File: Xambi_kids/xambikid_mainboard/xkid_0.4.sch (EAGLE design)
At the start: 18 parts

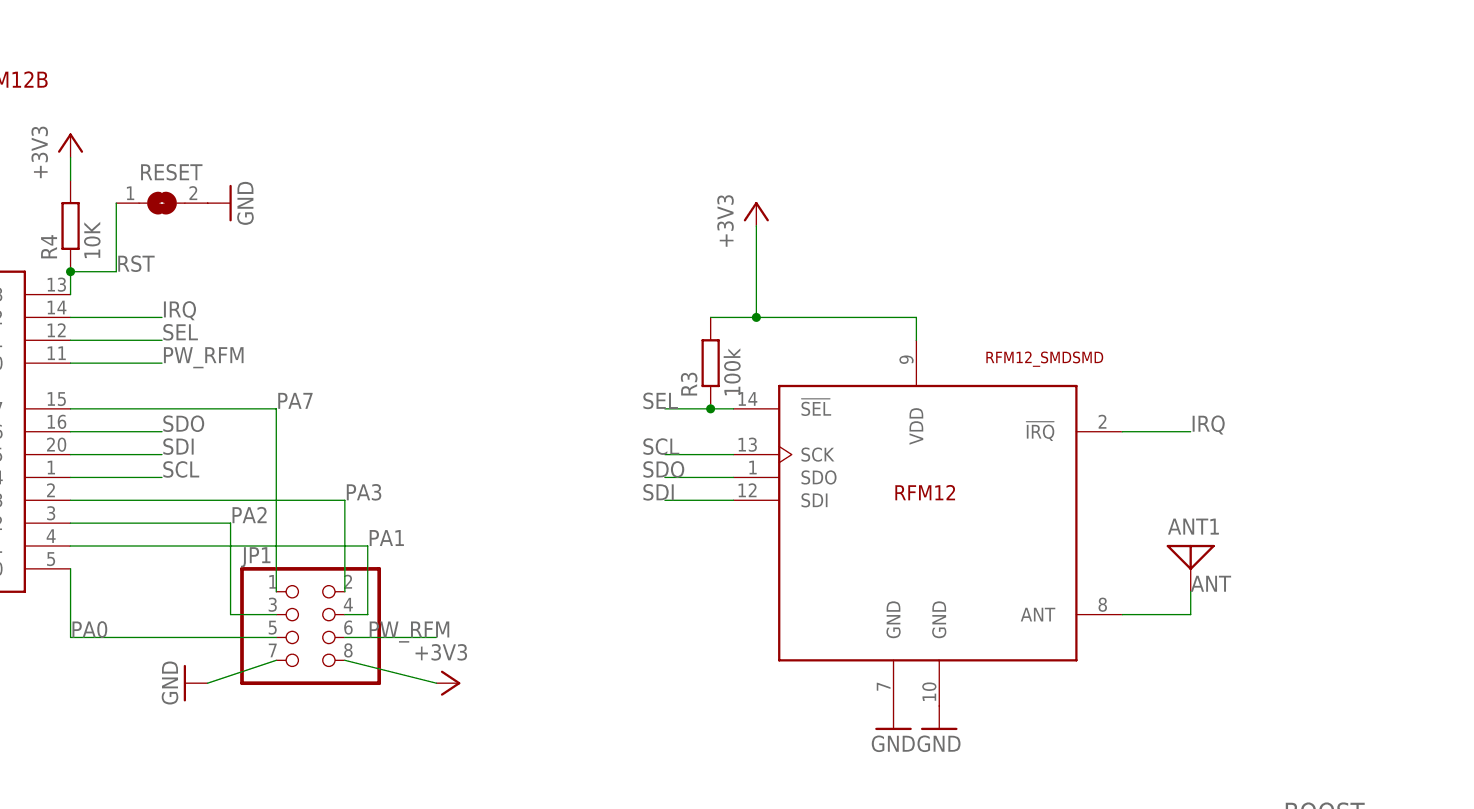
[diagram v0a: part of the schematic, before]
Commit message: - Add readme and pics to new board with booster and infrared
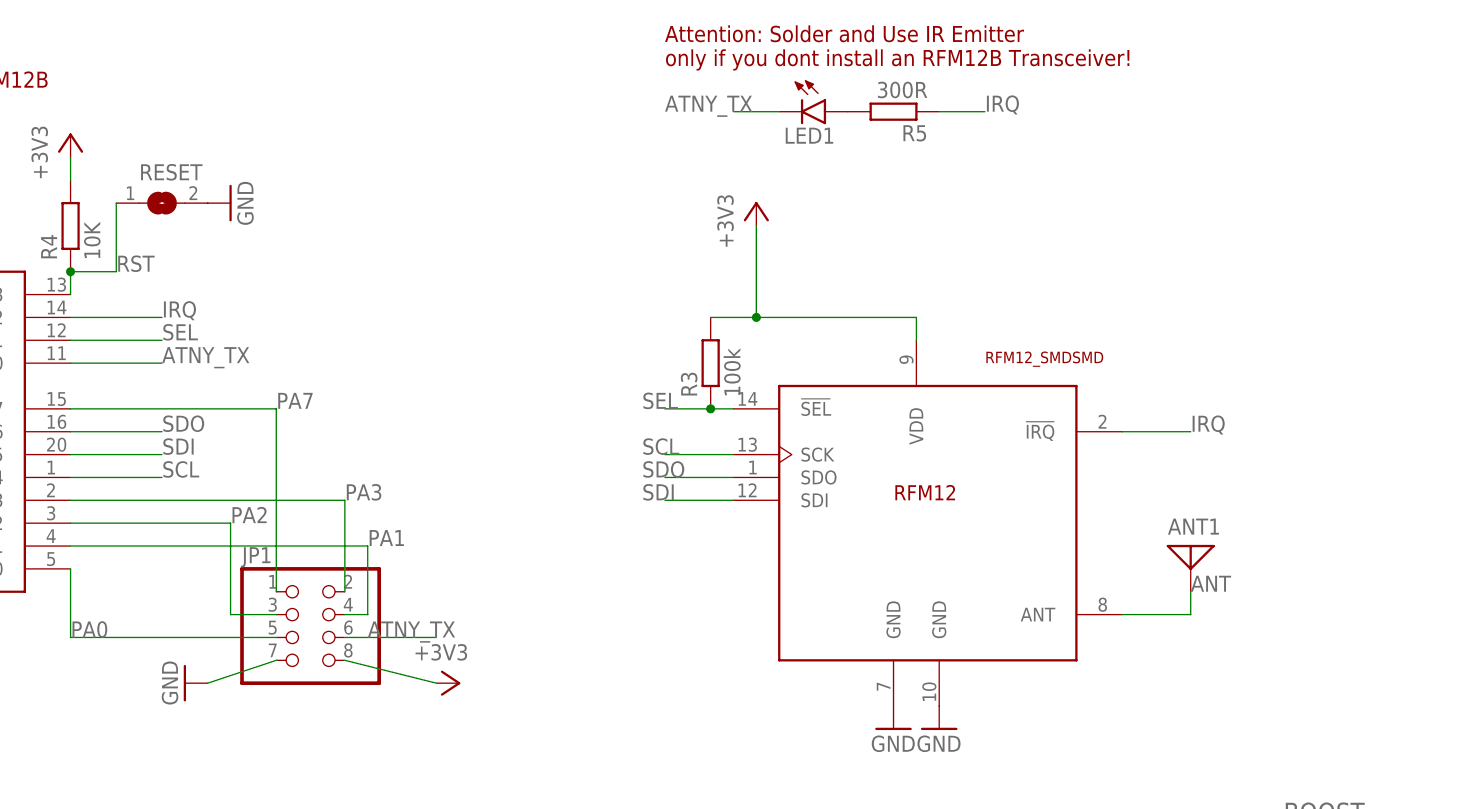
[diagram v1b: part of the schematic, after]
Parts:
- added LED1: (no value), SparkFun-LED:LED3MM
- added R5: 300R, rcl:R-EU_R0805
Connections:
- new net ATNY_TX: JP1.6, LED1.C, TINY84.(PCINT8/XTAL1/CLKI)PB0
- new net N$1: LED1.A, R5.2
- net IRQ: now also R5.1
- net PW_RFM: no longer JP1.6, TINY84.(PCINT8/XTAL1/CLKI)PB0
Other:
- note added: "Attention: Solder and Use IR Emitter only if you dont install an RFM12B Transceiver!"
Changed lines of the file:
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@@
 <?xml version="1.0" encoding="utf-8"?>
 <!DOCTYPE eagle SYSTEM "eagle.dtd">
-<eagle version="7.1.0">
+<eagle version="7.2.0">
 <drawing>
 <settings>
@@
 <part name="C4" library="rcl" deviceset="C-EU" device="C0805K" value="4.7mF"/>
 <part name="C5" library="rcl" deviceset="C-EU" device="C0805K" value="4.7mF"/>
+<part name="LED1" library="SparkFun-LED" deviceset="LED" device="3MM"/>
+<part name="R5" library="rcl" deviceset="R-EU_" device="R0805" value="300R"/>
 </parts>
 <sheets>
@@
 <text x="10.16" y="101.6" size="1.778" layer="94">Xambi_kid an attiny84 low power with a coincell CR2032 and a RFM12B
 http://jeelabs.net/projects/hardware/wiki/JeeNode_Micro</text>
+<text x="157.48" y="106.68" size="1.778" layer="94">Attention: Solder and Use IR Emitter
+only if you dont install an RFM12B Transceiver!</text>
 </plain>
 <instances>
@@
 <instance part="C4" gate="G$1" x="261.62" y="7.62" rot="R180"/>
 <instance part="C5" gate="G$1" x="195.58" y="5.08" rot="R180"/>
+<instance part="LED1" gate="G$1" x="175.26" y="101.6" rot="R270"/>
+<instance part="R5" gate="G$1" x="182.88" y="101.6" rot="R180"/>
 </instances>
 <busses>
@@
 <pinref part="U$1" gate="U$1" pin="!IRQ"/>
 </segment>
+<segment>
+<pinref part="R5" gate="G$1" pin="1"/>
+<wire x1="187.96" y1="101.6" x2="193.04" y2="101.6" width="0.1524" layer="91"/>
+<label x="193.04" y="101.6" size="1.778" layer="95"/>
+</segment>
 </net>
 <net name="RST" class="0">
@@
 </net>
 <net name="PW_RFM" class="0">
-<segment>
-<wire x1="91.44" y1="73.66" x2="101.6" y2="73.66" width="0.1524" layer="91"/>
-<label x="101.6" y="73.66" size="1.778" layer="95"/>
-<pinref part="TINY84" gate="G$1" pin="(PCINT8/XTAL1/CLKI)PB0"/>
-</segment>
-<segment>
-<pinref part="JP1" gate="A" pin="6"/>
-<wire x1="121.92" y1="43.18" x2="132.08" y2="43.18" width="0.1524" layer="91"/>
-<label x="124.46" y="43.18" size="1.778" layer="95"/>
-</segment>
 <segment>
 <pinref part="BOOST" gate="A" pin="VOUT"/>
@@
 </segment>
 </net>
+<net name="N$1" class="0">
+<segment>
+<pinref part="LED1" gate="G$1" pin="A"/>
+<pinref part="R5" gate="G$1" pin="2"/>
+</segment>
+</net>
+<net name="ATNY_TX" class="0">
+<segment>
+<wire x1="91.44" y1="73.66" x2="101.6" y2="73.66" width="0.1524" layer="91"/>
+<label x="101.6" y="73.66" size="1.778" layer="95"/>
+<pinref part="TINY84" gate="G$1" pin="(PCINT8/XTAL1/CLKI)PB0"/>
+</segment>
+<segment>
+<pinref part="JP1" gate="A" pin="6"/>
+<wire x1="121.92" y1="43.18" x2="132.08" y2="43.18" width="0.1524" layer="91"/>
+<label x="124.46" y="43.18" size="1.778" layer="95"/>
+</segment>
+<segment>
+<pinref part="LED1" gate="G$1" pin="C"/>
+<wire x1="170.18" y1="101.6" x2="165.1" y2="101.6" width="0.1524" layer="91"/>
+<label x="157.48" y="101.6" size="1.778" layer="95"/>
+</segment>
+</net>

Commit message: add booster to mainboard, add IR LED for ir communication
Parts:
- removed RESET: (no value), jumper:SJ
- added BOOST_OFF: (no value), jumper:SJ
- added S1: SWITCH-MOMENTARY-2TACTILE-SWITCH-SMD-RIGHT-ANGLE, SparkFun-Electromechanical:SWITCH-MOMENTARY-2TACTILE-SWITCH-SMD-RIGHT-ANGLE
- IR: value (none) -> IR
- renumbered ANT1 to ANT, LED1 to IR
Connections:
- removed net BAT+: BOOST.EN, BOOST.VIN, C5.2, L1.2
- removed net PW_RFM: BOOST.VOUT, C2.2, C4.2, R2.2
- new net BOOST_POWER: BOOST.VOUT, BOOST_OFF.2, C2.2, C4.2, JP1.8, R2.2
- net +3V3: no longer JP1.8
- net GND: now also S1.2; no longer RESET.2
- net PA0: now also BOOST.EN, BOOST.VIN, BOOST_OFF.1, C5.2, L1.2
- net RST: now also S1.1; no longer RESET.1
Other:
- note added: "Attention: Power come over Pin PA0/D10/A0/AREF, this pin have to activate every time!"
